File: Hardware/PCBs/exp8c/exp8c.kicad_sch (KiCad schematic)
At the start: 5 parts, among them J1 Conn_01x05_Female, J2 Conn_01x02_Female, U1 7410, U2 7410, U3 7400

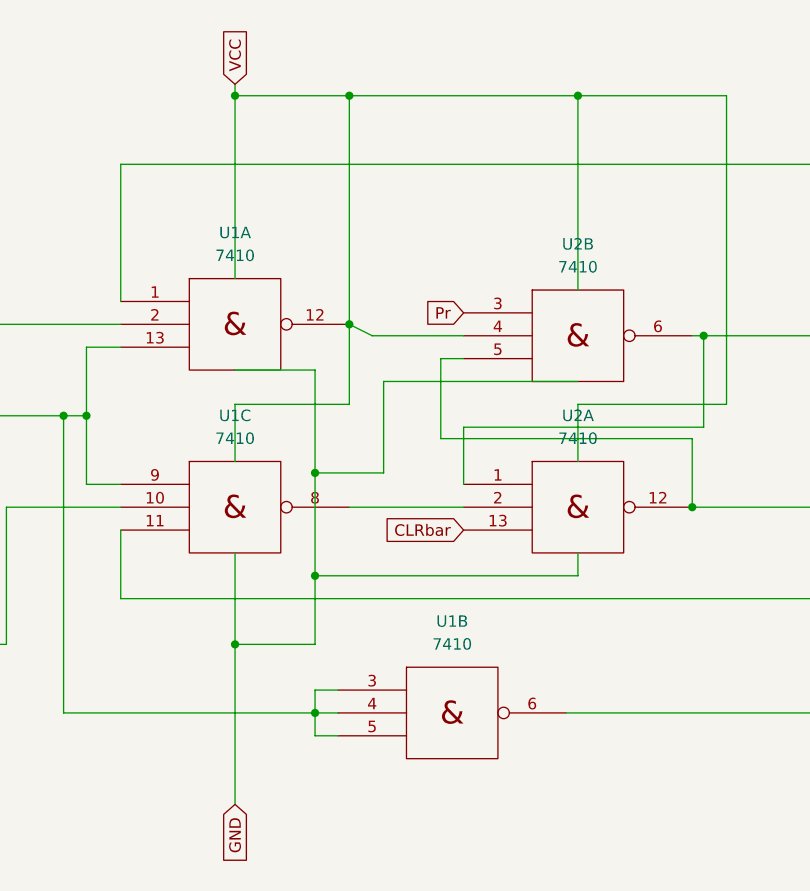
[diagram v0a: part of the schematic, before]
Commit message: Several PCBs updated
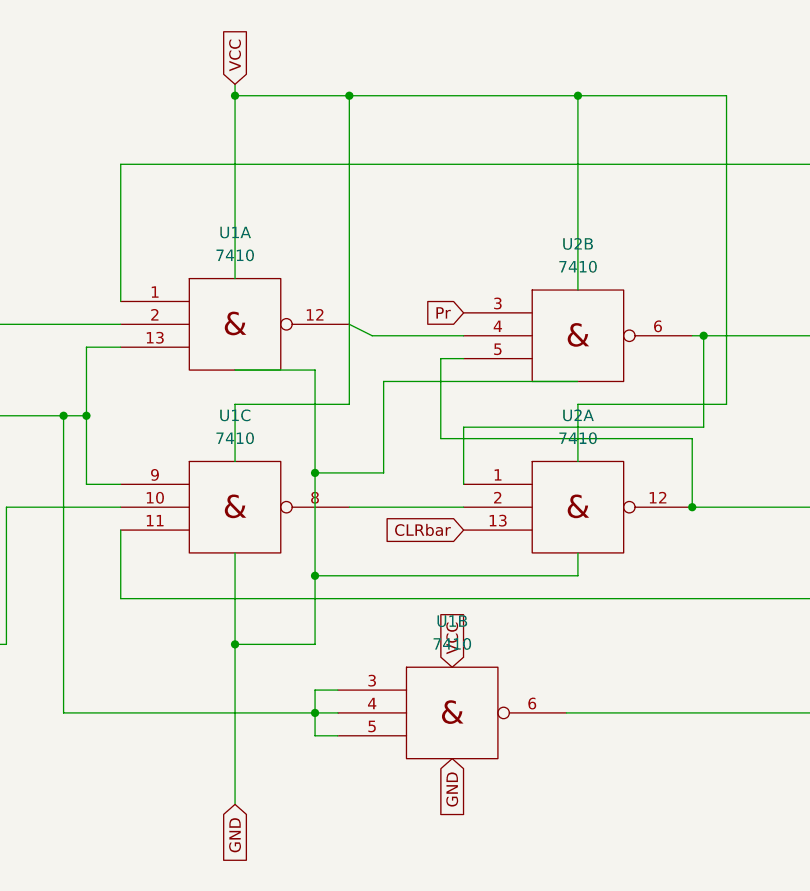
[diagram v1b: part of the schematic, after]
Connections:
- net Vcc: no longer U1.12, U2.4
- new net: U1.12, U2.4
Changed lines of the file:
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@@
   (junction (at 119.38 50.8) (diameter 0) (color 0 0 0 0)
   )
-  (junction (at 119.38 76.2) (diameter 0) (color 0 0 0 0)
-  )
   (junction (at 144.78 50.8) (diameter 0) (color 0 0 0 0)
   )
@@
     (stroke (width 0) (type default) (color 0 0 0 0))
   )
-  (wire (pts (xy 119.38 76.2) (xy 119.38 50.8))
-    (stroke (width 0) (type default) (color 0 0 0 0))
-  )
   (wire (pts (xy 62.23 76.2) (xy 62.23 111.76))
     (stroke (width 0) (type default) (color 0 0 0 0))
@@
     (stroke (width 0) (type default) (color 0 0 0 0))
   )
-  (wire (pts (xy 119.38 85.09) (xy 119.38 76.2))
+  (wire (pts (xy 119.38 50.8) (xy 119.38 85.09))
     (stroke (width 0) (type default) (color 0 0 0 0))
   )
@@
     )
   )
+  (global_label "VCC" (shape input) (at 130.81 114.3 90) (fields_autoplaced)
+    (effects (font (size 1.27 1.27)) (justify left))
+    (property "Intersheet References" "${INTERSHEET_REFS}" (id 0) (at 130.8894 108.2583 90)
+      (effects (font (size 1.27 1.27)) (justify left) hide)
+    )
+  )
   (global_label "VCC" (shape input) (at 226.06 121.92 180) (fields_autoplaced)
     (effects (font (size 1.27 1.27)) (justify right))
@@
     )
   )
+  (global_label "GND" (shape input) (at 130.81 124.46 270) (fields_autoplaced)
+    (effects (font (size 1.27 1.27)) (justify right))
+    (property "Intersheet References" "${INTERSHEET_REFS}" (id 0) (at 130.8894 130.7436 90)
+      (effects (font (size 1.27 1.27)) (justify right) hide)
+    )
+  )

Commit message: Multiple PCBs updated
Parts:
- added H1, H2, H3, H4: MountingHole, MountingHole:MountingHole_2.5mm, symbol Mechanical:MountingHole
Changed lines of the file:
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@@
     (pin "7")
+  )
+  (symbol (lib_id "Mechanical:MountingHole") (at 67.31 142.24 0) (unit 1)
+    (in_bom yes) (on_board yes) (fields_autoplaced)
+    (property "Reference" "H4" (id 0) (at 69.85 140.9699 0)
+      (effects (font (size 1.27 1.27)) (justify left))
+    )
+    (property "Value" "MountingHole" (id 1) (at 69.85 143.5099 0)
+      (effects (font (size 1.27 1.27)) (justify left))
+    )
+    (property "Footprint" "MountingHole:MountingHole_2.5mm" (id 2) (at 67.31 142.24 0)
+      (effects (font (size 1.27 1.27)) hide)
+    )
+    (property "Datasheet" "~" (id 3) (at 67.31 142.24 0)
+      (effects (font (size 1.27 1.27)) hide)
+    )
   )
   (symbol (lib_id "74xx:7400") (at 238.76 121.92 90) (unit 5)
@@
     (pin "9")
   )
+  (symbol (lib_id "Mechanical:MountingHole") (at 62.23 127 0) (unit 1)
+    (in_bom yes) (on_board yes) (fields_autoplaced)
+    (property "Reference" "H3" (id 0) (at 64.77 125.7299 0)
+      (effects (font (size 1.27 1.27)) (justify left))
+    )
+    (property "Value" "MountingHole" (id 1) (at 64.77 128.2699 0)
+      (effects (font (size 1.27 1.27)) (justify left))
+    )
+    (property "Footprint" "MountingHole:MountingHole_2.5mm" (id 2) (at 62.23 127 0)
+      (effects (font (size 1.27 1.27)) hide)
+    )
+    (property "Datasheet" "~" (id 3) (at 62.23 127 0)
+      (effects (font (size 1.27 1.27)) hide)
+    )
+  )
   (symbol (lib_id "74xx_IEEE:7410") (at 106.68 76.2 0) (unit 1)
     (in_bom yes) (on_board yes) (fields_autoplaced)
@@
     (pin "9")
   )
+  (symbol (lib_id "Mechanical:MountingHole") (at 43.18 139.7 0) (unit 1)
+    (in_bom yes) (on_board yes) (fields_autoplaced)
+    (property "Reference" "H1" (id 0) (at 45.72 138.4299 0)
+      (effects (font (size 1.27 1.27)) (justify left))
+    )
+    (property "Value" "MountingHole" (id 1) (at 45.72 140.9699 0)
+      (effects (font (size 1.27 1.27)) (justify left))
+    )
+    (property "Footprint" "MountingHole:MountingHole_2.5mm" (id 2) (at 43.18 139.7 0)
+      (effects (font (size 1.27 1.27)) hide)
+    )
+    (property "Datasheet" "~" (id 3) (at 43.18 139.7 0)
+      (effects (font (size 1.27 1.27)) hide)
+    )
+  )
+  (symbol (lib_id "Mechanical:MountingHole") (at 55.88 120.65 0) (unit 1)
+    (in_bom yes) (on_board yes) (fields_autoplaced)
+    (property "Reference" "H2" (id 0) (at 58.42 119.3799 0)
+      (effects (font (size 1.27 1.27)) (justify left))
+    )
+    (property "Value" "MountingHole" (id 1) (at 58.42 121.9199 0)
+      (effects (font (size 1.27 1.27)) (justify left))
+    )
+    (property "Footprint" "MountingHole:MountingHole_2.5mm" (id 2) (at 55.88 120.65 0)
+      (effects (font (size 1.27 1.27)) hide)
+    )
+    (property "Datasheet" "~" (id 3) (at 55.88 120.65 0)
+      (effects (font (size 1.27 1.27)) hide)
+    )
+  )
   (symbol (lib_id "74xx:7400") (at 200.66 77.47 0) (unit 1)
     (in_bom yes) (on_board yes) (fields_autoplaced)
@@
   )
   (symbol_instances
+    (path "/abf3b73e-032f-4479-a4b9-1ce597aa86c6"
+      (reference "H1") (unit 1) (value "MountingHole") (footprint "MountingHole:MountingHole_2.5mm")
+    )
+    (path "/c2ade15b-f699-4ae1-9bae-01fc10811013"
+      (reference "H2") (unit 1) (value "MountingHole") (footprint "MountingHole:MountingHole_2.5mm")
+    )
+    (path "/65f0fe12-62d6-4349-b981-34b0ed77624c"
+      (reference "H3") (unit 1) (value "MountingHole") (footprint "MountingHole:MountingHole_2.5mm")
+    )
+    (path "/27da16ae-ccd7-4e0e-a858-a15cfc968ce2"
+      (reference "H4") (unit 1) (value "MountingHole") (footprint "MountingHole:MountingHole_2.5mm")
+    )
     (path "/d17fd8a8-9785-407b-ad0e-2b5d879dbd6b"
       (reference "J1") (unit 1) (value "Conn_01x05_Female") (footprint "Connector_JST:JST_EH_S5B-EH_1x05_P2.50mm_Horizontal")
